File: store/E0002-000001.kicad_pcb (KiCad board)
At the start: 2 copper layers, 27 parts, among them J1 Power_IN, J2 Connector, J3 S0 input from DIN meter, J4 Leak sensor, J5 Door reed (NO), J6 Seansor_Header_A, J7 Seansor_Header_B, U1 TMP117xxDRV, U2 INA226

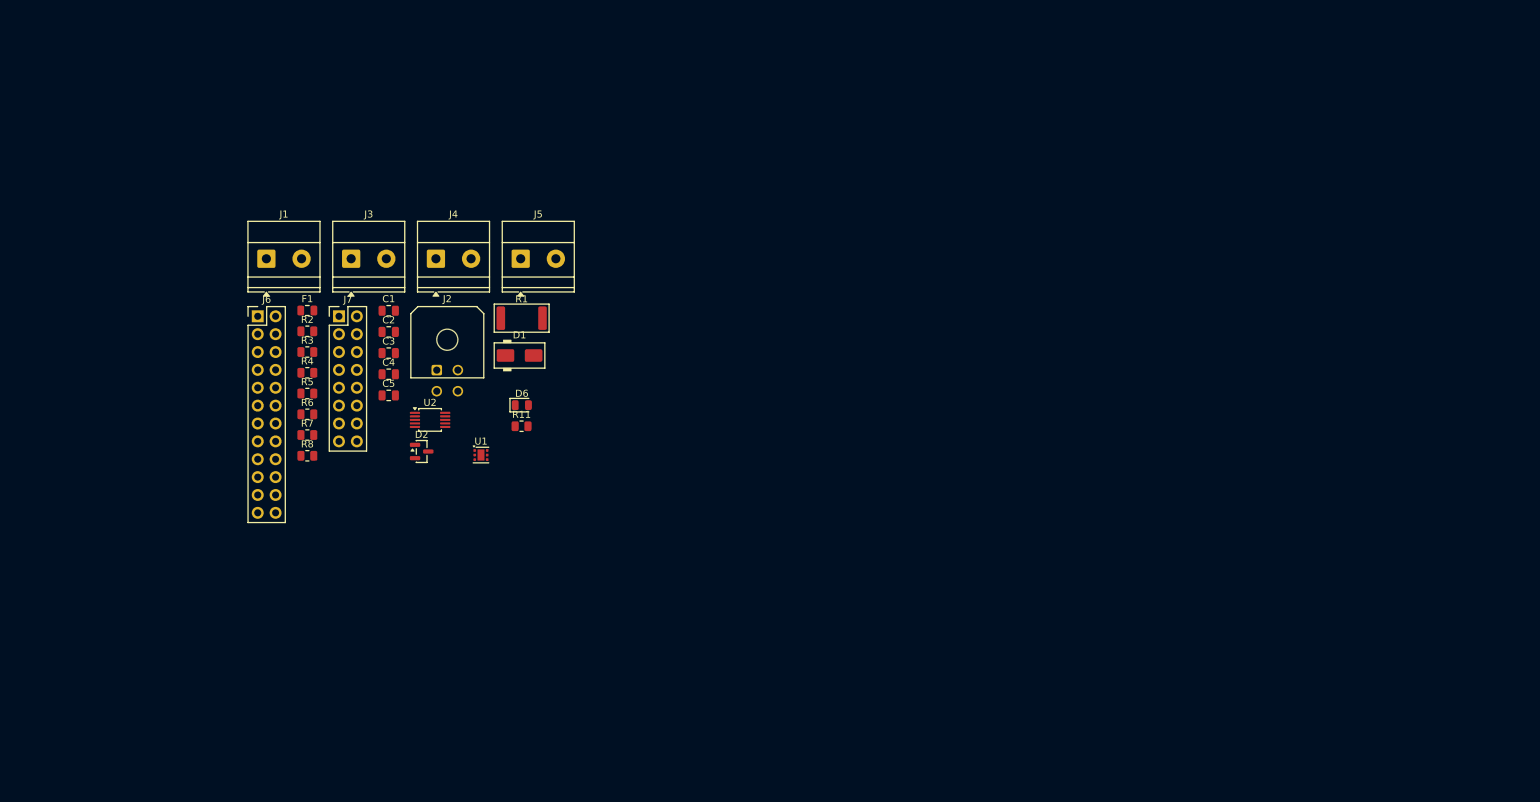
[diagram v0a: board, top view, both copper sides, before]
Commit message: feat(E0002): continue PCB layout and add footprint library table
- Update E0002 PCB layout, schematic, and project routing/designators
- Add store/fp-lib-table referencing the industrygrow footprint library
- Update active layer state in E0001/E0002 board settings

Signed-off-by: IIchukissII <133657307+IIchukissII@users.noreply.github.com>
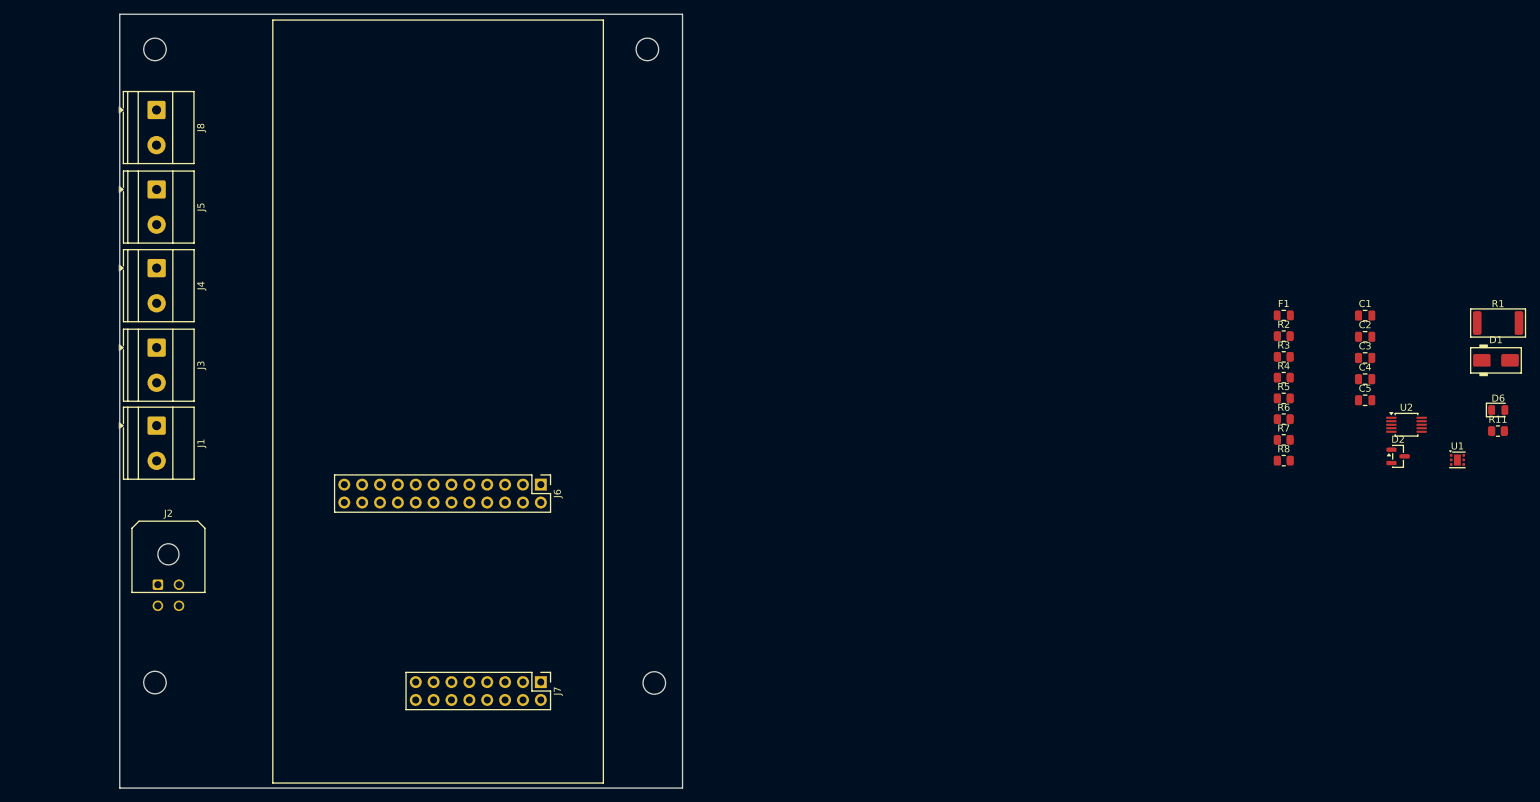
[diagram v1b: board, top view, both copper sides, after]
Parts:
- added J8: CAN input from Rasp, TerminalBlock_Phoenix:TerminalBlock_Phoenix_MKDS-1,5-2_1x02_P5.00mm_Horizontal, F.Cu at (55.2, 33.6)
- moved U1 138.8 mm to (240.1, 83.4)
- moved C1 138.8 mm to (227.0, 62.8)
- moved C2 138.8 mm to (227.0, 65.8)
- moved C3 138.8 mm to (227.0, 68.9)
- moved C4 138.8 mm to (227.0, 71.9)
- moved C5 138.8 mm to (227.0, 74.9)
- moved D1 138.8 mm to (245.6, 69.2)
- moved D2 138.8 mm to (231.7, 82.8)
- moved D6 138.8 mm to (246.0, 76.3)
- moved F1 138.8 mm to (215.5, 62.8)
- moved R1 138.8 mm to (245.9, 63.9)
- moved R11 138.8 mm to (245.9, 79.3)
- moved R2 138.8 mm to (215.5, 65.8)
- moved R3 138.8 mm to (215.5, 68.7)
- moved R4 138.8 mm to (215.5, 71.7)
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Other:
- board outline added: 80 x 110 mm

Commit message: feat(E0002): continue PCB layout and add GND on schematic
Signed-off-by: IIchukissII <133657307+IIchukissII@users.noreply.github.com>
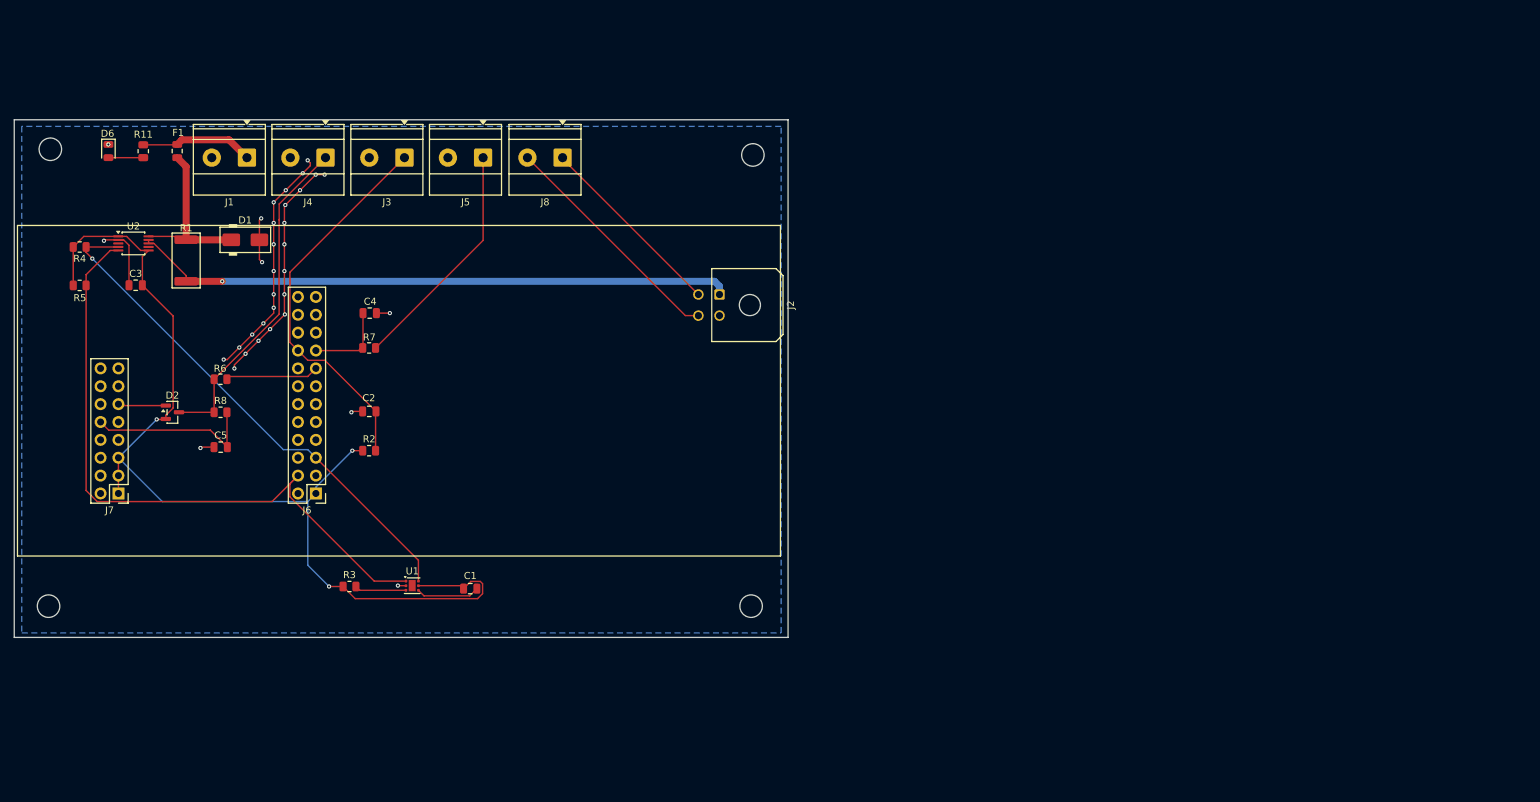
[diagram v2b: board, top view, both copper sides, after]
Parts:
- moved D6 201.0 mm to (48.4, 39.4), turned to -90 degrees
- moved R11 196.6 mm to (53.3, 39.5), turned to -90 degrees
- moved R1 186.7 mm to (59.4, 55.0), turned to -90 degrees
- moved U2 182.8 mm to (51.9, 52.6)
- moved D1 178.6 mm to (67.8, 52.1)
- moved C3 175.1 mm to (52.3, 58.5), turned to 180 degrees
- moved D2 174.3 mm to (57.5, 76.6)
- moved R4 172.2 mm to (44.3, 53.1), turned to 180 degrees
- moved R5 171.9 mm to (44.3, 58.5), turned to 180 degrees
- moved C5 162.8 mm to (64.3, 81.5)
- moved F1 159.0 mm to (58.2, 39.4), turned to -90 degrees
- moved R8 151.3 mm to (64.3, 76.6)
- moved R6 151.2 mm to (64.3, 71.9), turned to 180 degrees
- moved U1 149.7 mm to (91.6, 101.2)
- moved C2 142.0 mm to (85.5, 76.5), turned to 180 degrees
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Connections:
- U2 pad 7: STRAP_0 -> STRAP_1
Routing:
- net STRAP_0: track 0.00 -> 146.5 mm, vias 0 -> 3
- net STRAP_1: track 0.00 -> 106.3 mm, vias 0 -> 34
- net I2C1_SCL: track 0.00 -> 93.9 mm
- net Net-(J2-Pin_1): track 0.00 -> 85.9 mm, vias 0 -> 1
- net I2C1_SDA: track 0.00 -> 73.7 mm, vias 0 -> 1
- net GPIO_4: track 0.00 -> 54.9 mm
- net Net-(D2-COM): track 0.00 -> 47.7 mm
- net CAN_L: track 0.00 -> 33.6 mm
- net Net-(J5-Pin_1): track 0.00 -> 33.4 mm
- net CAN_H: track 0.00 -> 27.5 mm
- net ADC_1: track 0.00 -> 24.5 mm
- net Net-(D1-K): track 0.00 -> 24.1 mm
- net +12V: track 0.00 -> 16.1 mm
- net GPIO_1: track 0.00 -> 13.3 mm
- net GPIO_3: track 0.00 -> 11.8 mm
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- added copper zone on B.Cu, net STRAP_1
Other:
- board size 80 x 110 mm -> 110 x 73.6 mm

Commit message: feat(E0002): complete PCB layout
Finalize board layout for E0002-000001 and add board render (PNG).

Signed-off-by: IIchukissII <133657307+IIchukissII@users.noreply.github.com>
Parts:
- added G***: LOGO, LOGO, F.Cu at (54.8, 104.9)
- J3: value S0 input from DIN meter -> S0 input
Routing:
- net I2C1_SDA: track 73.7 -> 101.6 mm
- net Net-(J2-Pin_1): track 85.9 -> 93.2 mm, vias 1 -> 2
- net STRAP_1: track 106.3 -> 109.3 mm, vias 34 -> 36
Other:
- board text added: "E0002 V00.00.01"
- board text added: "SN:"
